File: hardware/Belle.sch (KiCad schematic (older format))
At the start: 22 parts, among them P1 Bell CONN, P2 Battery CONN, P3 FTDI Flashing CONN, U1 74AHC1G14, U2 ESP-12, U3 AP2112

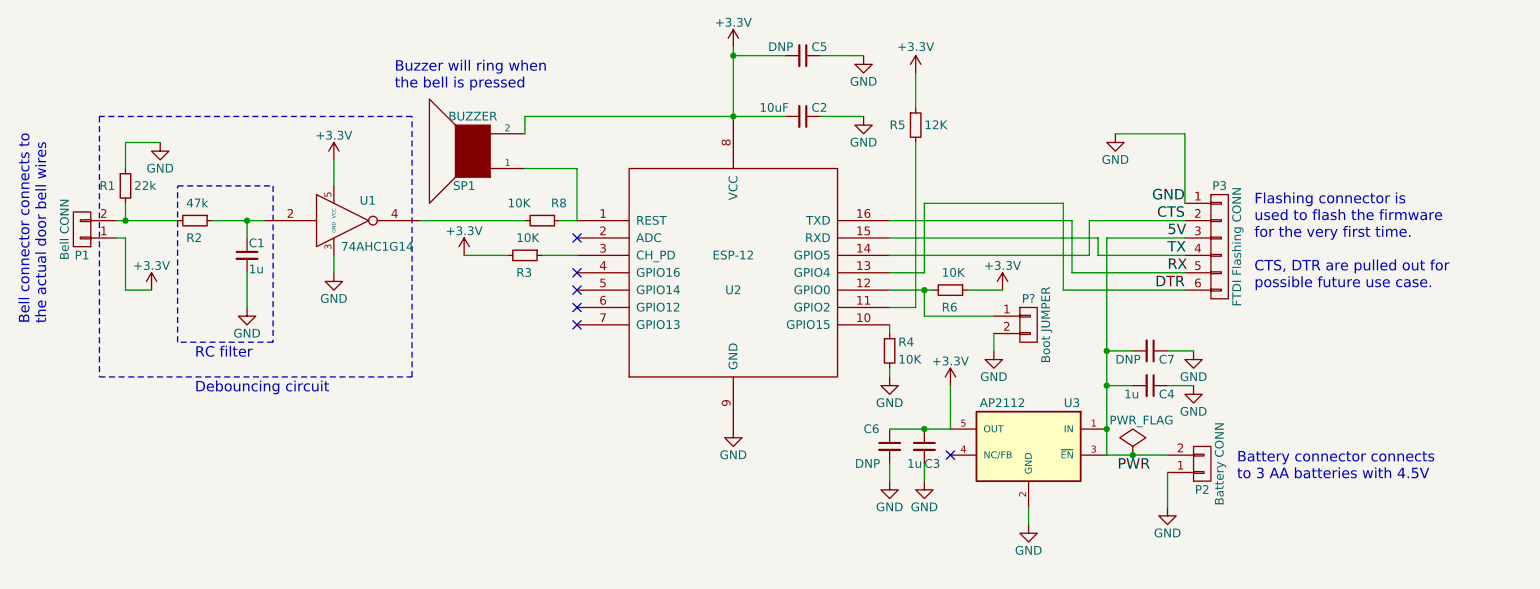
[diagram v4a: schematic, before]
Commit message: re-generate net list based on new schematic
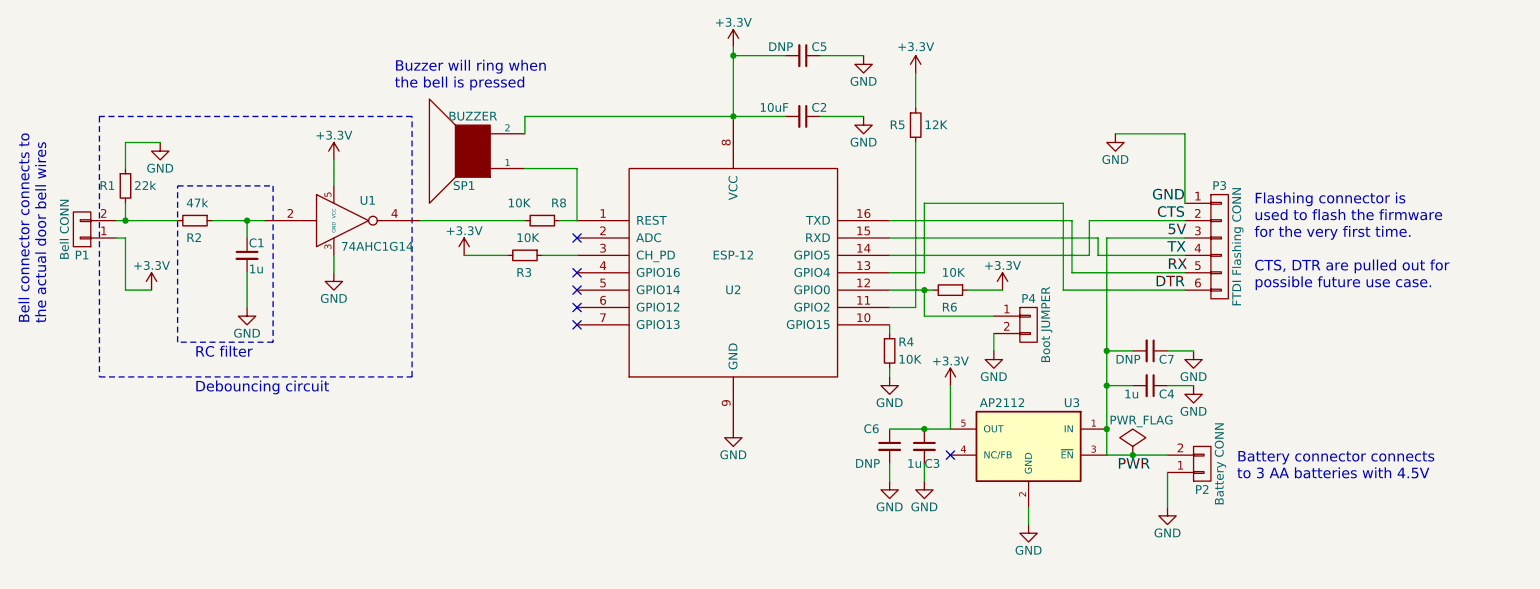
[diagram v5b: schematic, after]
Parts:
- C5, C6, C7: footprint (none) -> Capacitors_SMD:C_1206_HandSoldering
- P4: renamed from P?; footprint (none) -> Pin_Headers:Pin_Header_Straight_1x02_Pitch2.54mm
- R8: footprint (none) -> Resistors_SMD:R_1206_HandSoldering
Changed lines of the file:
@@
 	3600 3700 3600 3800
 Wire Wire Line
-	2900 3500 3100 3500
-Wire Wire Line
-	3100 3500 3200 3500
+	2900 3500 3200 3500
 Wire Wire Line
 	3100 3600 3100 3500
@@
 	3100 3800 3100 4000
 Wire Wire Line
-	2350 3500 2400 3500
-Wire Wire Line
-	2400 3500 2700 3500
+	2350 3500 2700 3500
 Wire Wire Line
 	4800 3700 5000 3700
@@
 	4600 3700 4350 3700
 Wire Wire Line
-	6800 3900 7000 3900
-Wire Wire Line
-	7000 3900 7050 3900
+	6800 3900 7050 3900
 Wire Wire Line
 	7250 3900 7450 3900
@@
 	7600 5150 7600 5250
 Wire Wire Line
-	8050 4850 8200 4850
-Wire Wire Line
-	8200 4850 8400 4850
-Wire Wire Line
-	8050 3600 8050 4250
-Wire Wire Line
-	8050 4250 8050 4450
-Wire Wire Line
-	8050 4450 8050 4700
-Wire Wire Line
-	8050 4700 8050 4850
+	8050 4850 8400 4850
+Wire Wire Line
+	8050 3600 8050 4850
 Wire Wire Line
 	8400 4950 8400 5150
@@
 F 0 "R8" V 4700 3550 50  0000 L CNN
 F 1 "10K" V 4700 3300 50  0000 L CNN
-F 2 "" H 4800 3500 50  0000 C CNN
+F 2 "Resistors_SMD:R_1206_HandSoldering" H 4800 3500 50  0001 C CNN
 F 3 "" H 4800 3500 50  0000 C CNN
 	1    4800 3500
@@
 	4700 3500 4100 3500
 Wire Wire Line
-	4700 2900 5900 2900
-Wire Wire Line
-	5900 2900 6200 2900
+	4700 2900 6200 2900
 $Comp
 L C_Small C5
@@
 F 0 "C5" V 6250 2600 50  0000 L CNN
 F 1 "DNP" V 6250 2350 50  0000 L CNN
-F 2 "" H 6300 2550 50  0000 C CNN
+F 2 "Capacitors_SMD:C_1206_HandSoldering" H 6300 2550 50  0001 C CNN
 F 3 "" H 6300 2550 50  0000 C CNN
 	1    6300 2550
@@
 $EndComp
 Wire Wire Line
-	5900 2500 5900 2550
-Wire Wire Line
-	5900 2550 5900 2900
+	5900 2500 5900 2900
 Wire Wire Line
 	6200 2550 5900 2550
@@
 F 0 "C7" V 8350 4300 50  0000 L CNN
 F 1 "DNP" V 8350 4050 50  0000 L CNN
-F 2 "" H 8300 4250 50  0000 C CNN
+F 2 "Capacitors_SMD:C_1206_HandSoldering" H 8300 4250 50  0001 C CNN
 F 3 "" H 8300 4250 50  0000 C CNN
 	1    8300 4250
@@
 F 0 "C6" H 6650 4900 50  0000 L CNN
 F 1 "DNP" H 6600 4700 50  0000 L CNN
-F 2 "" H 6800 4800 50  0000 C CNN
+F 2 "Capacitors_SMD:C_1206_HandSoldering" H 6800 4800 50  0001 C CNN
 F 3 "" H 6800 4800 50  0000 C CNN
 	1    6800 4800
@@
 	7000 4900 7000 5000
 Wire Wire Line
-	6800 4700 7000 4700
-Wire Wire Line
-	7000 4700 7150 4700
+	6800 4700 7150 4700
 Connection ~ 7000 4700
 Wire Wire Line
@@
 	8500 3000 8100 3000
 $Comp
-L CONN_01X02 P?
+L CONN_01X02 P4
 U 1 1 59074415
 P 7600 4100
-F 0 "P?" H 7600 4250 50  0000 C CNN
+F 0 "P4" H 7600 4250 50  0000 C CNN
 F 1 "Boot JUMPER" V 7700 4100 50  0000 C CNN
-F 2 "" H 7600 4100 50  0000 C CNN
+F 2 "Pin_Headers:Pin_Header_Straight_1x02_Pitch2.54mm" H 7600 4100 50  0001 C CNN
 F 3 "" H 7600 4100 50  0000 C CNN
 	1    7600 4100
@@
 Connection ~ 7000 3900
 $Comp
-L GND #PWR?
+L GND #PWR023
 U 1 1 59074532
 P 7400 4250
-F 0 "#PWR?" H 7400 4000 50  0001 C CNN
+F 0 "#PWR023" H 7400 4000 50  0001 C CNN
 F 1 "GND" H 7400 4100 50  0000 C CNN
 F 2 "" H 7400 4250 50  0000 C CNN
@@
 	7950 3700 7950 3500
 Wire Wire Line
-	7950 3500 8300 3500
-Wire Wire Line
-	8300 3500 8300 3500
-Wire Wire Line
-	8300 3500 8500 3500
+	7950 3500 8500 3500
 Wire Wire Line
 	6800 3800 7000 3800

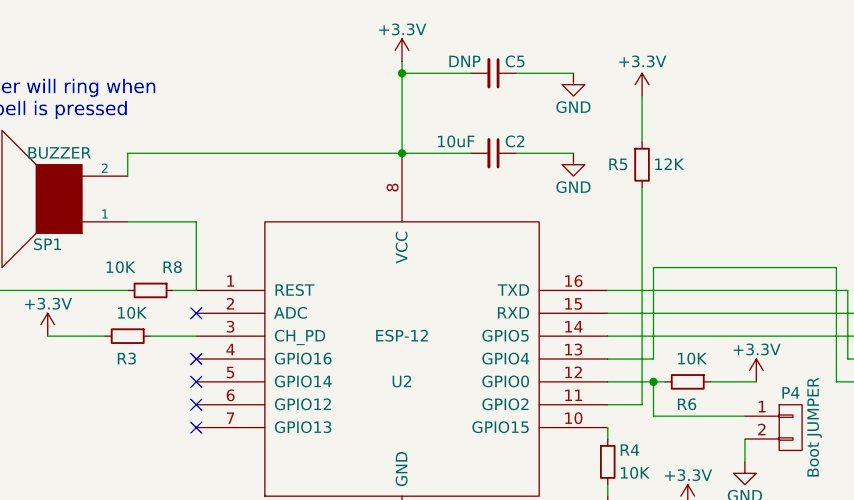
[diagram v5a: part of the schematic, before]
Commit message: generate bill of materials
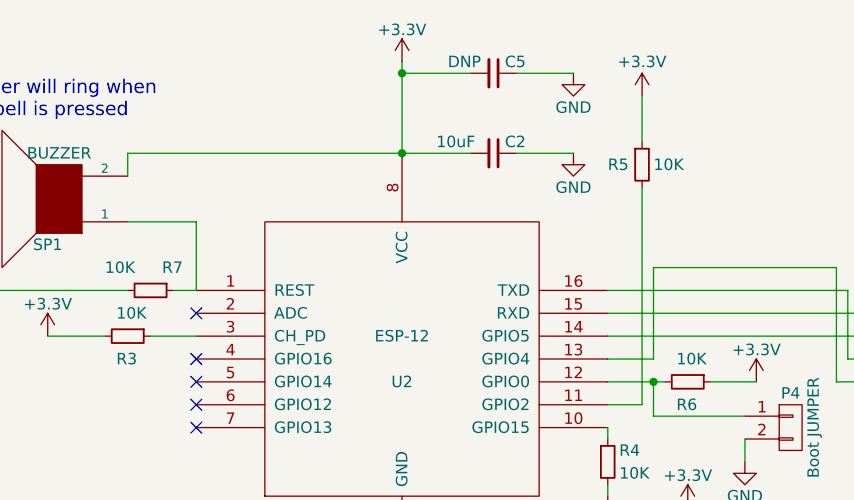
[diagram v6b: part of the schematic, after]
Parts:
- R5: value 12K -> 10K
- renumbered R8 to R7
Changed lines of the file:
@@
 P 6950 2950
 F 0 "R5" H 6800 2950 50  0000 L CNN
-F 1 "12K" H 7000 2950 50  0000 L CNN
+F 1 "10K" H 7000 2950 50  0000 L CNN
 F 2 "Resistors_SMD:R_1206_HandSoldering" H 6950 2950 50  0001 C CNN
 F 3 "" H 6950 2950 50  0000 C CNN
@@
 	2400 3900 2550 3900
 $Comp
-L R_Small R8
+L R_Small R7
 U 1 1 58FE989D
 P 4800 3500
-F 0 "R8" V 4700 3550 50  0000 L CNN
+F 0 "R7" V 4700 3550 50  0000 L CNN
 F 1 "10K" V 4700 3300 50  0000 L CNN
 F 2 "Resistors_SMD:R_1206_HandSoldering" H 4800 3500 50  0001 C CNN

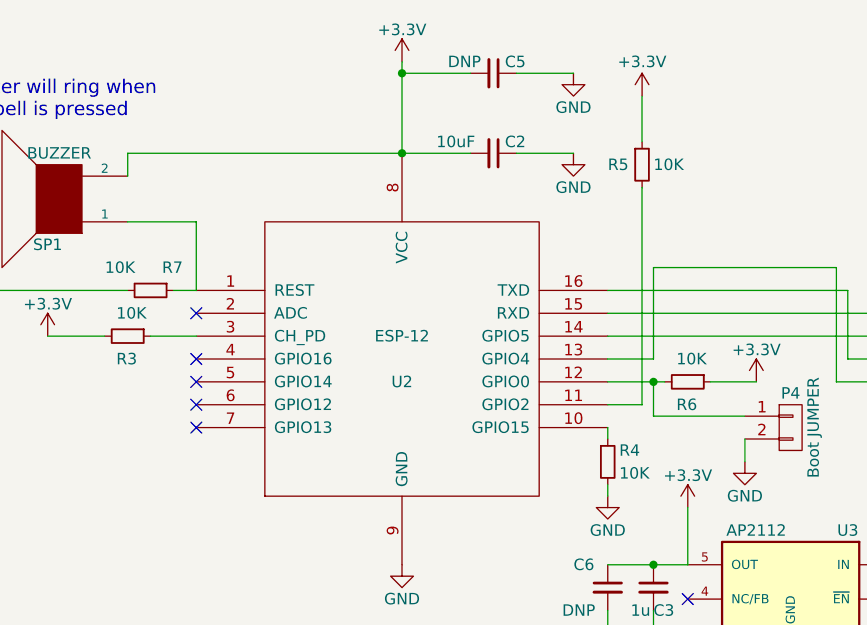
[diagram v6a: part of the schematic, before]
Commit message: rename resistors in order of schematic placement
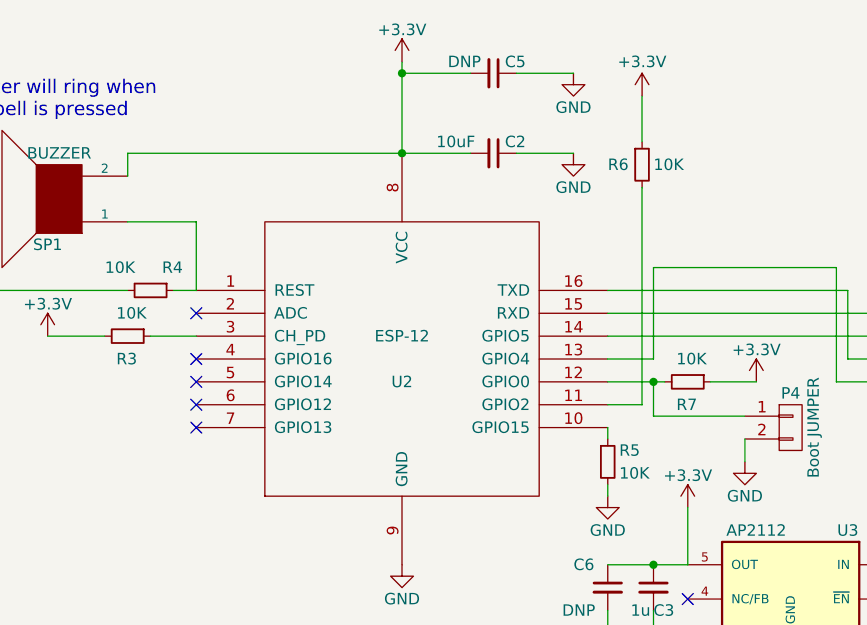
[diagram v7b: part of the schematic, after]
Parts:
- renumbered R7 to R4, R4 to R5, R5 to R6, R6 to R7
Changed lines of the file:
@@
 $EndComp
 $Comp
-L R_Small R6
+L R_Small R7
 U 1 1 58BBD5DC
 P 7150 3900
-F 0 "R6" V 7250 3850 50  0000 L CNN
+F 0 "R7" V 7250 3850 50  0000 L CNN
 F 1 "10K" V 7050 3850 50  0000 L CNN
 F 2 "Resistors_SMD:R_1206_HandSoldering" H 7150 3900 50  0001 C CNN
@@
 $EndComp
 $Comp
-L R_Small R4
+L R_Small R5
 U 1 1 58BBD6F3
 P 6800 4250
-F 0 "R4" H 6850 4300 50  0000 L CNN
+F 0 "R5" H 6850 4300 50  0000 L CNN
 F 1 "10K" H 6850 4200 50  0000 L CNN
 F 2 "Resistors_SMD:R_1206_HandSoldering" H 6800 4250 50  0001 C CNN
@@
 RX
 $Comp
-L R_Small R5
+L R_Small R6
 U 1 1 58BBEC6E
 P 6950 2950
-F 0 "R5" H 6800 2950 50  0000 L CNN
+F 0 "R6" H 6800 2950 50  0000 L CNN
 F 1 "10K" H 7000 2950 50  0000 L CNN
 F 2 "Resistors_SMD:R_1206_HandSoldering" H 6950 2950 50  0001 C CNN
@@
 	2400 3900 2550 3900
 $Comp
-L R_Small R7
+L R_Small R4
 U 1 1 58FE989D
 P 4800 3500
-F 0 "R7" V 4700 3550 50  0000 L CNN
+F 0 "R4" V 4700 3550 50  0000 L CNN
 F 1 "10K" V 4700 3300 50  0000 L CNN
 F 2 "Resistors_SMD:R_1206_HandSoldering" H 4800 3500 50  0001 C CNN

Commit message: add gerber files
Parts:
- C2: value 10uF -> DNP
- C4: value 1u -> DNP
- C5: value DNP -> 10u
- C7: value DNP -> 1u
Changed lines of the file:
@@
 P 6300 2900
 F 0 "C2" V 6250 2950 50  0000 L CNN
-F 1 "10uF" V 6250 2650 50  0000 L CNN
+F 1 "DNP" V 6250 2650 50  0000 L CNN
 F 2 "Capacitors_SMD:C_1206_HandSoldering" H 6300 2900 50  0001 C CNN
 F 3 "" H 6300 2900 50  0000 C CNN
@@
 P 8300 4450
 F 0 "C4" V 8350 4500 50  0000 L CNN
-F 1 "1u" V 8350 4300 50  0000 L CNN
+F 1 "DNP" V 8350 4300 50  0000 L CNN
 F 2 "Capacitors_SMD:C_1206_HandSoldering" H 8300 4450 50  0001 C CNN
 F 3 "" H 8300 4450 50  0000 C CNN
@@
 P 6300 2550
 F 0 "C5" V 6250 2600 50  0000 L CNN
-F 1 "DNP" V 6250 2350 50  0000 L CNN
+F 1 "10u" V 6250 2350 50  0000 L CNN
 F 2 "Capacitors_SMD:C_1206_HandSoldering" H 6300 2550 50  0001 C CNN
 F 3 "" H 6300 2550 50  0000 C CNN
@@
 P 8300 4250
 F 0 "C7" V 8350 4300 50  0000 L CNN
-F 1 "DNP" V 8350 4050 50  0000 L CNN
+F 1 "1u" V 8350 4050 50  0000 L CNN
 F 2 "Capacitors_SMD:C_1206_HandSoldering" H 8300 4250 50  0001 C CNN
 F 3 "" H 8300 4250 50  0000 C CNN
